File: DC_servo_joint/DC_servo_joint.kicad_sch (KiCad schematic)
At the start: 48 parts, among them U1 AS5600, U2 ESP32-C3-WROOM-02, U3 SP3485EN, U5 TPS563200

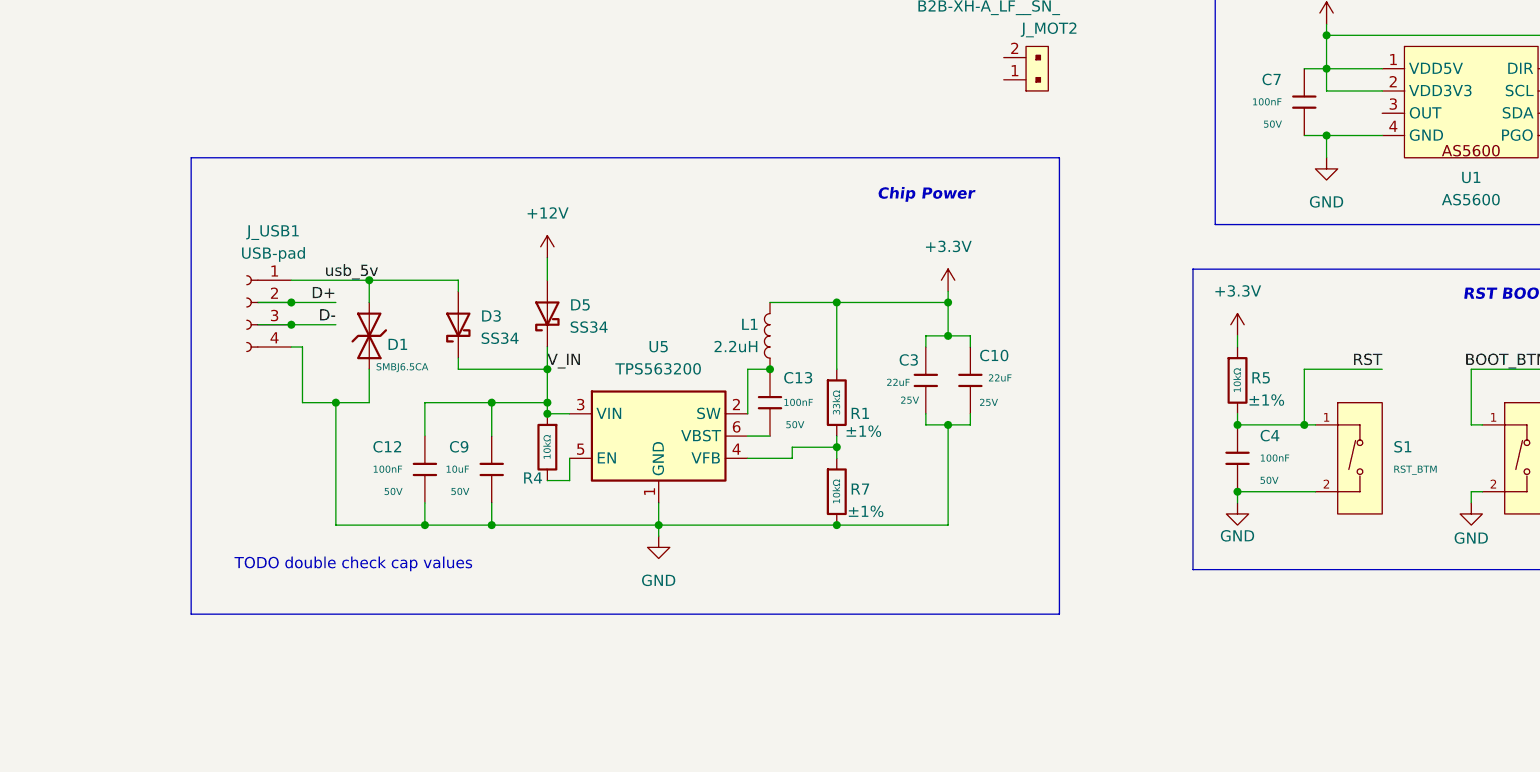
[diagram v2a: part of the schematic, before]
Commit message: Update the usb header to 8 pins,
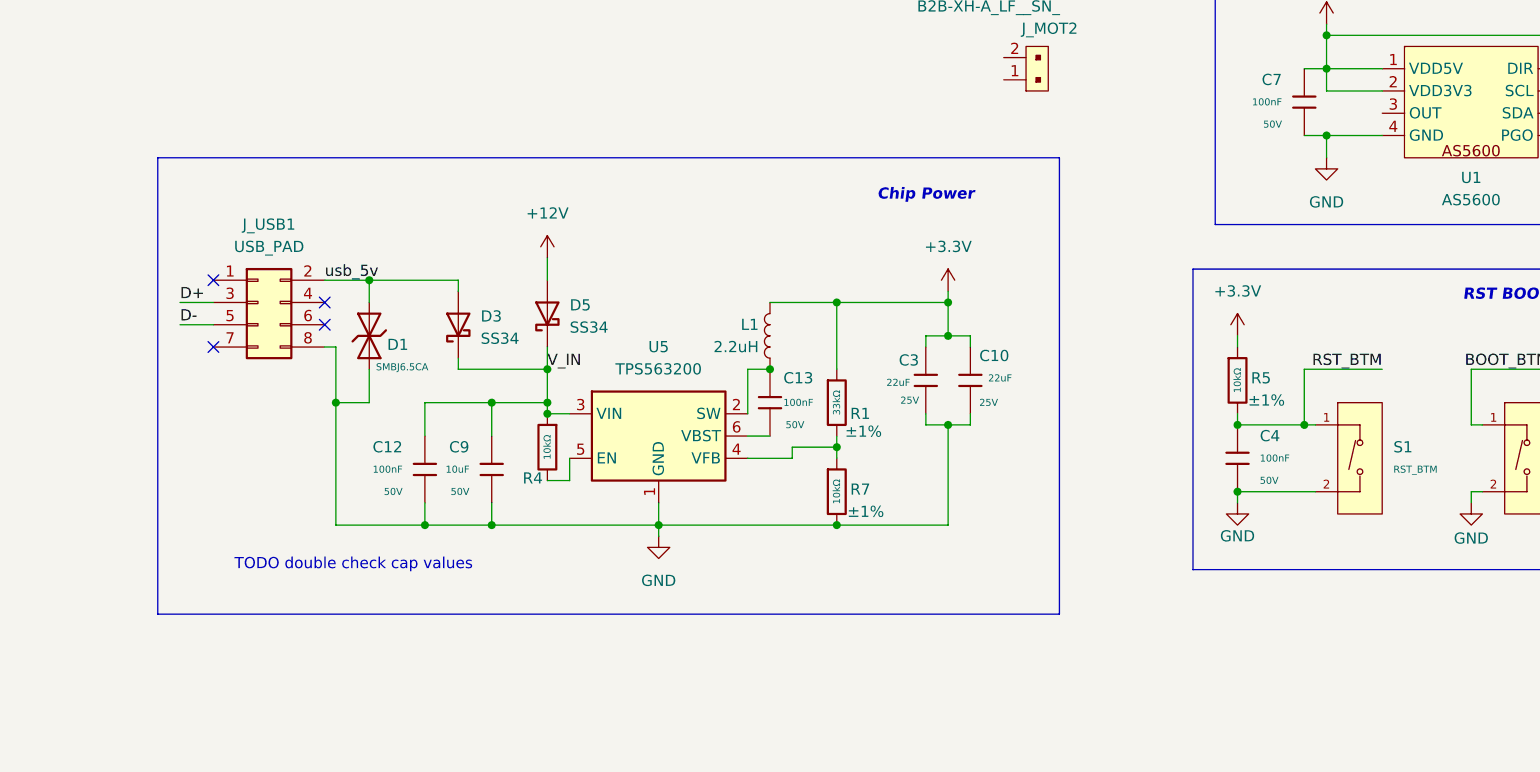
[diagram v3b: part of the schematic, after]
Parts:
- removed J_USB1: USB-pad, symbol Connector:Conn_01x04_Socket
- added J_USB1: USB_PAD, Connector_PinHeader_2.54mm:PinHeader_2x04_P2.54mm_Vertical, symbol Connector_Generic:Conn_02x04_Odd_Even
- C11: footprint (none) -> Capacitor_SMD:CP_Elec_6.3x5.4
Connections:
- net RST is gone; now on net RST_BTM: C4.1, R5.2, S1.1 (A)
- net D+: now also J_USB1.3 (Pin_3)
- net D-: now also J_USB1.5 (Pin_5)
- net GND: now also J_USB1.8 (Pin_8)
- net usb_5v: now also J_USB1.2 (Pin_2)
- no-connect marks 1 -> 5
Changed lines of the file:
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@@
 	)
 	(rectangle
-		(start 113.03 109.22)
+		(start 109.22 109.22)
 		(end 212.09 161.29)
 		(stroke
@@
 	)
 	(junction
-		(at 124.46 125.73)
-		(diameter 0)
-		(color 0 0 0 0)
-	)
-	(junction
 		(at 186.69 151.13)
 		(diameter 0)
@@
 	)
 	(junction
-		(at 124.46 128.27)
-		(diameter 0)
-		(color 0 0 0 0)
-	)
-	(junction
 		(at 153.67 133.35)
 		(diameter 0)
@@
 		(at 269.24 106.68)
 	)
+	(no_connect
+		(at 128.27 128.27)
+	)
+	(no_connect
+		(at 115.57 130.81)
+	)
+	(no_connect
+		(at 115.57 123.19)
+	)
+	(no_connect
+		(at 128.27 125.73)
+	)
 	(wire
 		(pts
@@
 	(wire
 		(pts
+			(xy 129.54 130.81) (xy 128.27 130.81)
+		)
+		(stroke
+			(width 0)
+			(type default)
+		)
+	)
+	(wire
+		(pts
 			(xy 163.83 39.37) (xy 163.83 44.45)
 		)
@@
 	(wire
 		(pts
-			(xy 129.54 137.16) (xy 125.73 137.16)
-		)
-		(stroke
-			(width 0)
-			(type default)
-		)
-	)
-	(wire
-		(pts
 			(xy 255.27 48.26) (xy 255.27 49.53)
 		)
@@
 	(wire
 		(pts
-			(xy 125.73 130.81) (xy 125.73 137.16)
+			(xy 129.54 130.81) (xy 129.54 137.16)
 		)
 		(stroke
@@
 	(wire
 		(pts
-			(xy 124.46 125.73) (xy 129.54 125.73)
-		)
-		(stroke
-			(width 0)
-			(type default)
-		)
-	)
-	(wire
-		(pts
 			(xy 114.3 72.39) (xy 127 72.39)
 		)
@@
 	(wire
 		(pts
-			(xy 120.65 125.73) (xy 124.46 125.73)
+			(xy 111.76 128.27) (xy 115.57 128.27)
 		)
 		(stroke
@@
 	(wire
 		(pts
-			(xy 120.65 128.27) (xy 124.46 128.27)
-		)
-		(stroke
-			(width 0)
-			(type default)
-		)
-	)
-	(wire
-		(pts
 			(xy 162.56 39.37) (xy 163.83 39.37)
 		)
@@
 	(wire
 		(pts
+			(xy 111.76 125.73) (xy 115.57 125.73)
+		)
+		(stroke
+			(width 0)
+			(type default)
+		)
+	)
+	(wire
+		(pts
 			(xy 184.15 36.83) (xy 184.15 35.56)
 		)
@@
 	(wire
 		(pts
+			(xy 128.27 123.19) (xy 133.35 123.19)
+		)
+		(stroke
+			(width 0)
+			(type default)
+		)
+	)
+	(wire
+		(pts
 			(xy 242.57 95.25) (xy 242.57 99.06)
 		)
@@
 	(wire
 		(pts
-			(xy 125.73 130.81) (xy 124.46 130.81)
-		)
-		(stroke
-			(width 0)
-			(type default)
-		)
-	)
-	(wire
-		(pts
 			(xy 269.24 95.25) (xy 242.57 95.25)
 		)
@@
 	(wire
 		(pts
-			(xy 124.46 123.19) (xy 133.35 123.19)
-		)
-		(stroke
-			(width 0)
-			(type default)
-		)
-	)
-	(wire
-		(pts
 			(xy 186.69 151.13) (xy 199.39 151.13)
 		)
@@
 	(wire
 		(pts
-			(xy 124.46 128.27) (xy 129.54 128.27)
-		)
-		(stroke
-			(width 0)
-			(type default)
-		)
-	)
-	(wire
-		(pts
 			(xy 186.69 125.73) (xy 199.39 125.73)
 		)
@@
 	)
 	(label "D+"
-		(at 129.54 125.73 180)
+		(at 111.76 125.73 0)
 		(effects
 			(font
 				(size 1.27 1.27)
 			)
-			(justify right bottom)
+			(justify left bottom)
 		)
 	)
@@
 	)
 	(label "D-"
-		(at 129.54 128.27 180)
+		(at 111.76 128.27 0)
 		(effects
 			(font
 				(size 1.27 1.27)
 			)
-			(justify right bottom)
+			(justify left bottom)
 		)
 	)
@@
 		)
 	)
-	(label "RST"
-		(at 248.92 133.35 180)
-		(effects
-			(font
-				(size 1.27 1.27)
-			)
-			(justify right bottom)
-		)
-	)
 	(label "UART_RX"
 		(at 62.23 110.49 0)
@@
 		)
 	)
+	(label "RST_BTM"
+		(at 248.92 133.35 180)
+		(effects
+			(font
+				(size 1.27 1.27)
+			)
+			(justify right bottom)
+		)
+	)
 	(label "NTC_PIN"
 		(at 256.54 57.15 0)
@@
 	)
 	(symbol
-		(lib_id "Connector:Conn_01x04_Socket")
-		(at 119.38 125.73 0)
-		(mirror y)
+		(lib_id "power:GND")
+		(at 232.41 148.59 0)
 		(unit 1)
 		(exclude_from_sim no)
@@
 		(on_board yes)
 		(dnp no)
-		(property "Reference" "J_USB1"
-			(at 122.428 117.602 0)
+		(property "Reference" "#PWR014"
+			(at 232.41 154.94 0)
 			(effects
 				(font
 					(size 1.27 1.27)
 				)
+				(hide yes)
 			)
 		)
-		(property "Value" "USB-pad"
-			(at 122.428 120.142 0)
+		(property "Value" "GND"
+			(at 232.41 152.4 0)
 			(effects
 				(font
@@
 		)
 		(property "Footprint" ""
-			(at 119.38 125.73 0)
+			(at 232.41 148.59 0)
 			(effects
 				(font
@@
 			)
 		)
-		(property "Datasheet" "~"
-			(at 119.38 125.73 0)
+		(property "Datasheet" ""
+			(at 232.41 148.59 0)
 			(effects
 				(font
@@
 			)
 		)
-		(property "Description" "Generic connector, single row, 01x04, script generated"
-			(at 119.38 125.73 0)
+		(property "Description" "Power symbol creates a global label with name \"GND\" , ground"
+			(at 232.41 148.59 0)
 			(effects
 				(font
@@
 			)
 		)
-		(pin "4"
-		)
-		(pin "2"
-		)
-		(pin "3"
-		)
 		(pin "1"
 		)
 		(instances
-			(project ""
+			(project "DC_servo_joint"
 				(path "/c8f8ac5e-0b71-42b6-88d1-0b81b7fe4cbf"
-					(reference "J_USB1")
+					(reference "#PWR014")
 					(unit 1)
 				)
@@
 	)
 	(symbol
-		(lib_id "power:GND")
-		(at 232.41 148.59 0)
+		(lib_id "Connector_Generic:Conn_02x04_Odd_Even")
+		(at 120.65 125.73 0)
 		(unit 1)
 		(exclude_from_sim no)
@@
 		(on_board yes)
 		(dnp no)
-		(property "Reference" "#PWR014"
-			(at 232.41 154.94 0)
+		(fields_autoplaced yes)
+		(property "Reference" "J_USB1"
+			(at 121.92 116.84 0)
 			(effects
 				(font
 					(size 1.27 1.27)
 				)
-				(hide yes)
 			)
 		)
-		(property "Value" "GND"
-			(at 232.41 152.4 0)
+		(property "Value" "USB_PAD"
+			(at 121.92 119.38 0)
 			(effects
 				(font
@@
 			)
 		)
-		(property "Footprint" ""
-			(at 232.41 148.59 0)
+		(property "Footprint" "Connector_PinHeader_2.54mm:PinHeader_2x04_P2.54mm_Vertical"
+			(at 120.65 125.73 0)
 			(effects
 				(font
@@
 			)
 		)
-		(property "Datasheet" ""
-			(at 232.41 148.59 0)
+		(property "Datasheet" "~"
+			(at 120.65 125.73 0)
 			(effects
 				(font
@@
 			)
 		)
-		(property "Description" "Power symbol creates a global label with name \"GND\" , ground"
-			(at 232.41 148.59 0)
+		(property "Description" "Generic connector, double row, 02x04, odd/even pin numbering scheme (row 1 odd numbers, row 2 even numbers), script generated (kicad-library-utils/schlib/autogen/connector/)"
+			(at 120.65 125.73 0)
 			(effects
 				(font
@@
 			)
 		)
+		(pin "4"
+		)
+		(pin "8"
+		)
+		(pin "3"
+		)
+		(pin "2"
+		)
+		(pin "5"
+		)
 		(pin "1"
 		)
+		(pin "6"
+		)
+		(pin "7"
+		)
 		(instances
-			(project "DC_servo_joint"
+			(project ""
 				(path "/c8f8ac5e-0b71-42b6-88d1-0b81b7fe4cbf"
-					(reference "#PWR014")
+					(reference "J_USB1")
 					(unit 1)
 				)
@@
 			)
 		)
-		(property "Footprint" ""
+		(property "Footprint" "Capacitor_SMD:CP_Elec_6.3x5.4"
 			(at 184.15 39.37 0)
 			(effects

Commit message: Started Power source layout
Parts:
- removed J_MOT2: B2B-XH-A_LF__SN_, digikey-footprints:PinHeader_1x2_P2.5mm_Drill1.1mm, symbol dk_Rectangular-Connectors-Headers-Male-Pins:B2B-XH-A_LF__SN_
- removed L1: 2.2uH, symbol Device:L
- added L2: 2.2uH,50mA, PCM_JLCPCB:L_0805, symbol PCM_JLCPCB-Inductors:2.2uH,50mA
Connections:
- net +3.3V: now also L2.1
- net TPS_SW: now reaches C13.1, U5.2 (SW)
- net TPS_SW: now also L2.2

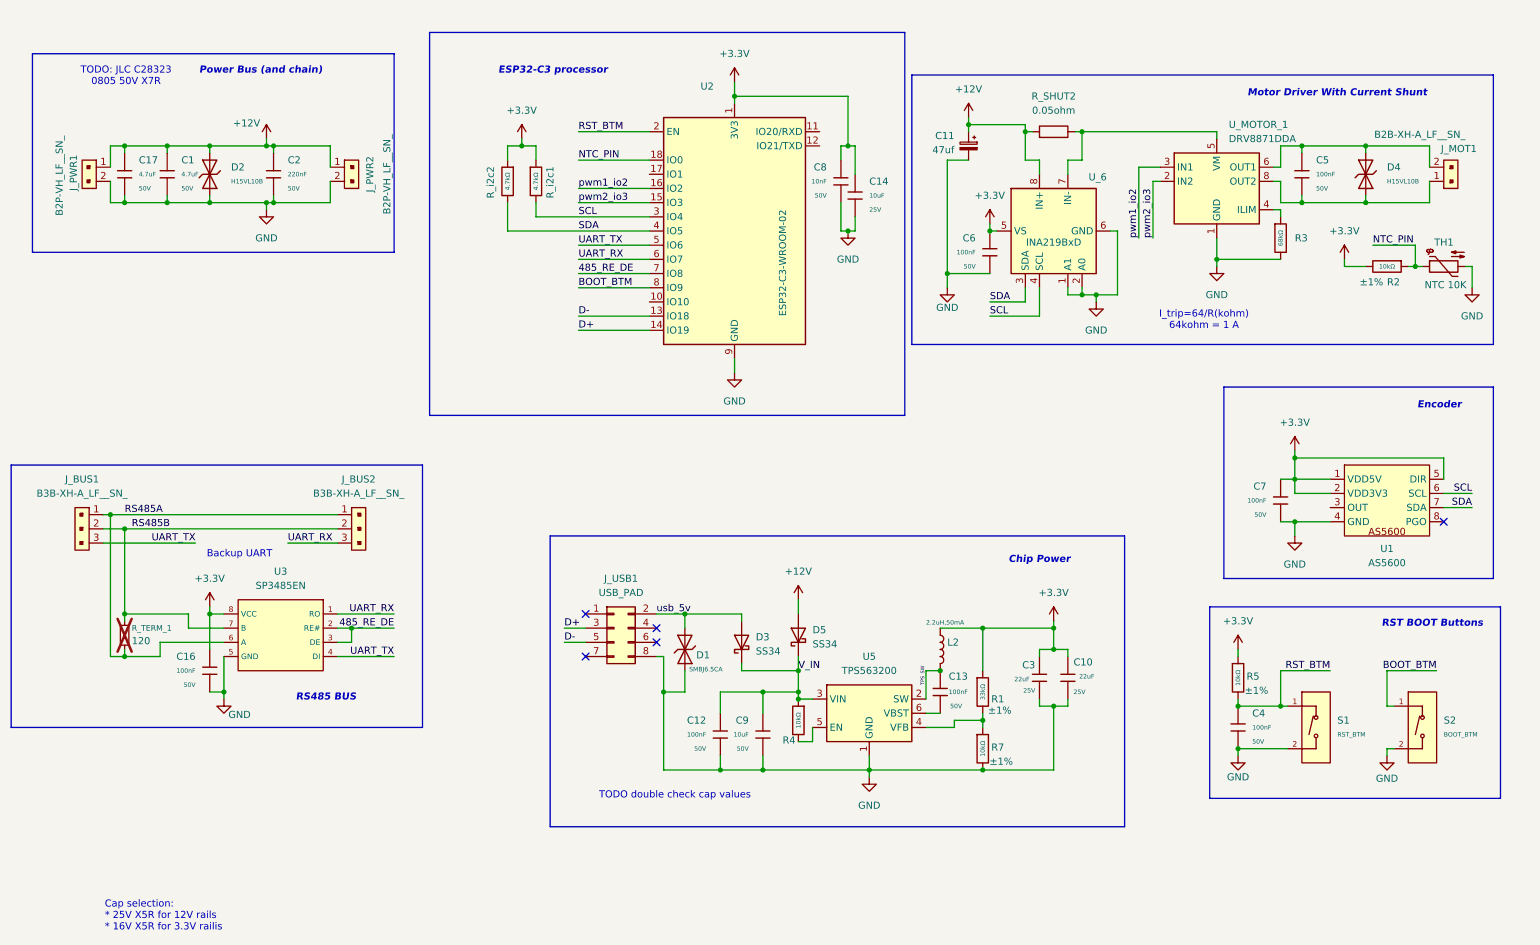
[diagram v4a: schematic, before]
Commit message: Most layout are in shape
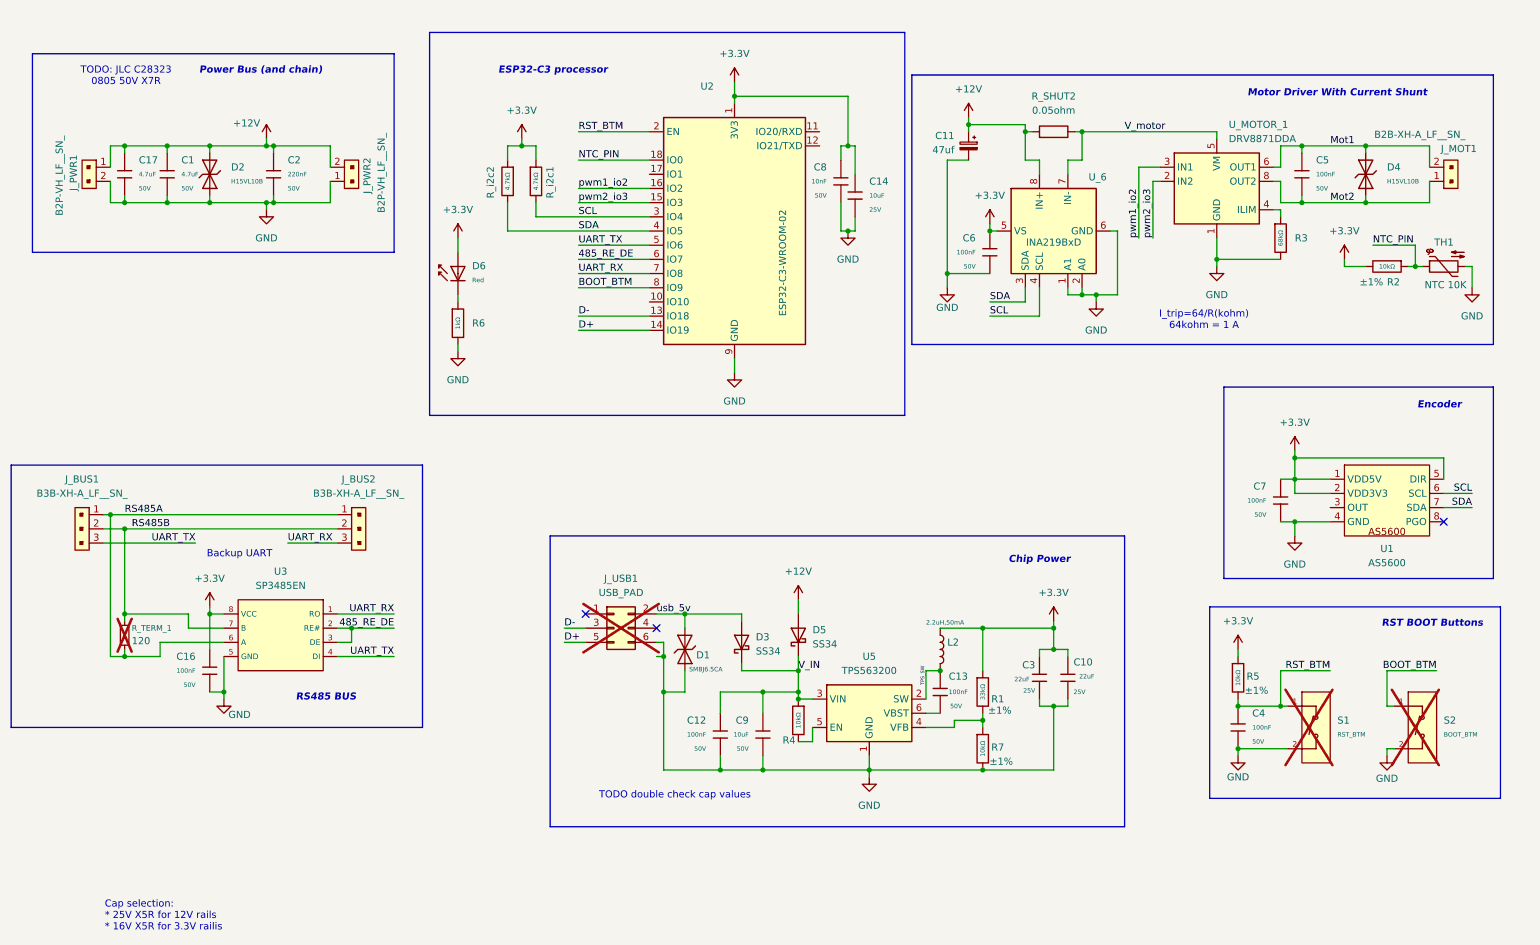
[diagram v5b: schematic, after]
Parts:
- removed J_USB1: USB_PAD, Connector_PinHeader_2.54mm:PinHeader_2x04_P2.54mm_Vertical, symbol Connector_Generic:Conn_02x04_Odd_Even
- added D6: Red, PCM_JLCPCB:D_0603, symbol PCM_JLCPCB-Diodes:LED,0603,Red
- added J_USB1: USB_PAD, Connector_PinSocket_2.54mm:PinSocket_2x03_P2.54mm_Vertical, symbol Connector_Generic:Conn_02x03_Odd_Even
- added R6: 1kΩ, PCM_JLCPCB:R_0402, symbol PCM_JLCPCB-Resistors:0402,1kΩ
- J_BUS1, J_BUS2: footprint digikey-footprints:PinHeader_1x3_P2.5mm_Drill1.1mm -> Connector_JST:JST_XH_S3B-XH-A_1x03_P2.50mm_Horizontal
- J_MOT1: footprint digikey-footprints:PinHeader_1x2_P2.5mm_Drill1.1mm -> Connector_JST:JST_XH_S2B-XH-A_1x02_P2.50mm_Horizontal
- J_PWR1, J_PWR2: footprint digikey-footprints:PinHeader_1x2_P3.96mm_Drill1.6mm -> Connector_JST:JST_VH_S2P-VH_1x02_P3.96mm_Horizontal
- S1, S2: now not fitted
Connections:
- net +12V: now also J_PWR2.2; no longer J_PWR2.1
- net +3.3V: now also D6.2
- net 485_RE_DE: now also U2.6 (IO7); no longer U2.7 (IO8)
- net D+: now also J_USB1.5 (Pin_5)
- net D-: now also J_USB1.3 (Pin_3)
- net GND: now also J_PWR2.1, J_USB1.6 (Pin_6), R6.2; no longer J_PWR2.2
- net UART_RX: now also U2.7 (IO8); no longer U2.6 (IO7)
- net usb_5v: now also J_USB1.2 (Pin_2)
- net Mot1: now reaches C5.1, D4.2, J_MOT1.2, U_MOTOR_1.6 (OUT1)
- net Mot2: now reaches C5.2, D4.1, J_MOT1.1, U_MOTOR_1.8 (OUT2)
- net V_motor: now reaches R_SHUT2.1, U_6.7 (IN-), U_MOTOR_1.5 (VM)
- new net: D6.1, R6.1
- no-connect marks 5 -> 3

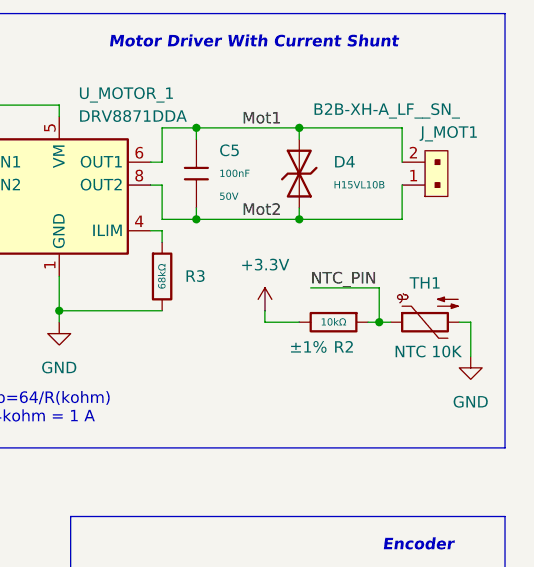
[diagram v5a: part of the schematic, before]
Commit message: Fixed missing tarce, added in some skilscreen fix
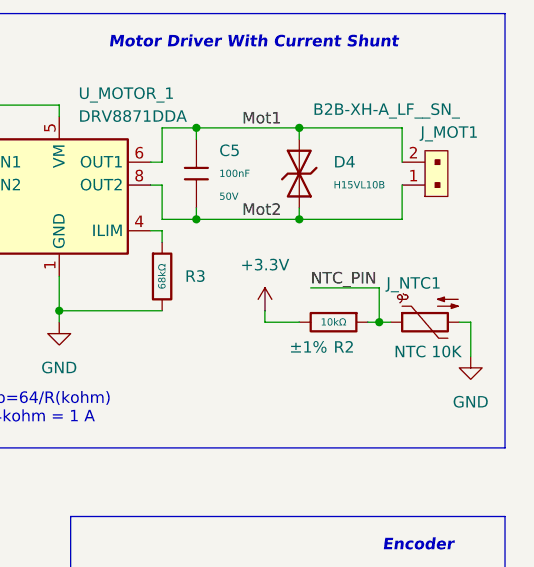
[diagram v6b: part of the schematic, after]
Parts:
- renumbered TH1 to J_NTC1
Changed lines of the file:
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@@
 		(on_board yes)
 		(dnp no)
-		(property "Reference" "TH1"
+		(property "Reference" "J_NTC1"
 			(at 271.018 56.642 90)
 			(effects
@@
 			(project ""
 				(path "/c8f8ac5e-0b71-42b6-88d1-0b81b7fe4cbf"
-					(reference "TH1")
+					(reference "J_NTC1")
 					(unit 1)
 				)
